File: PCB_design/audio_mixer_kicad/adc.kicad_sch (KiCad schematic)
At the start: 10 parts, among them U10 TLV320ADC3140IRTWR

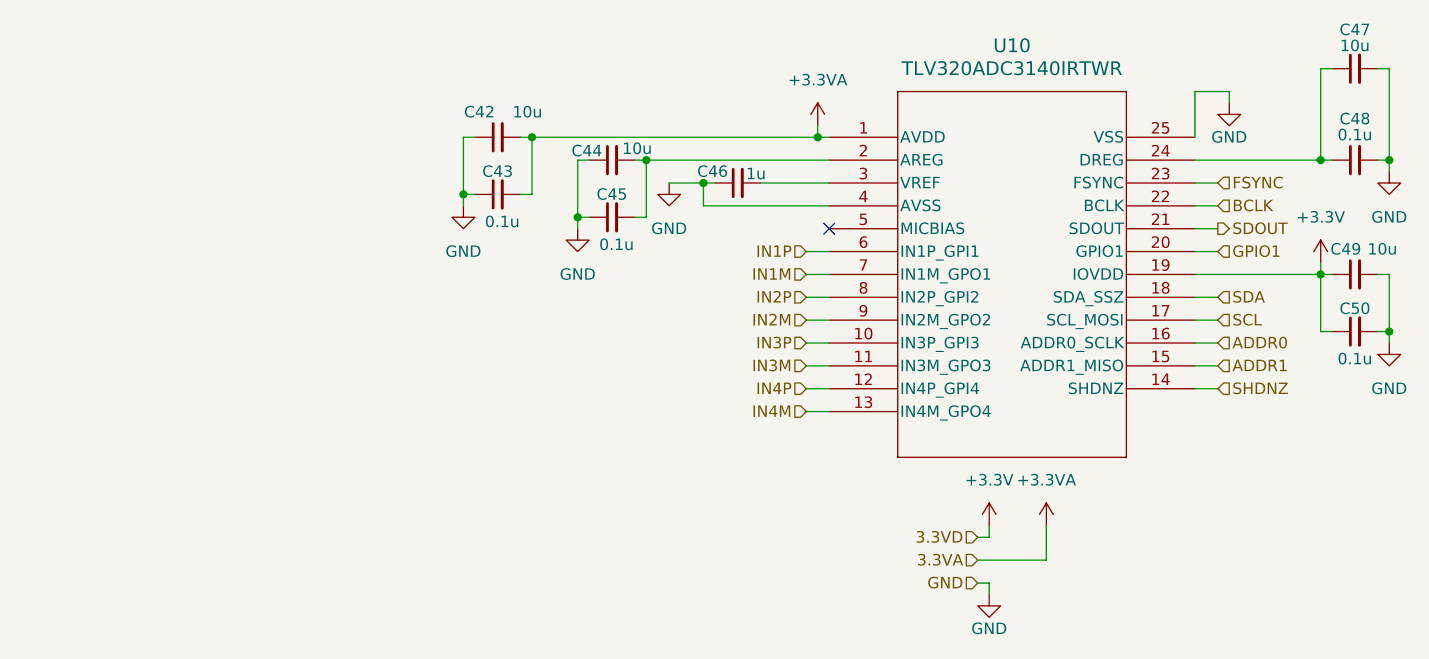
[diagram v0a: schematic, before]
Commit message: Add oscillator and adc input caps
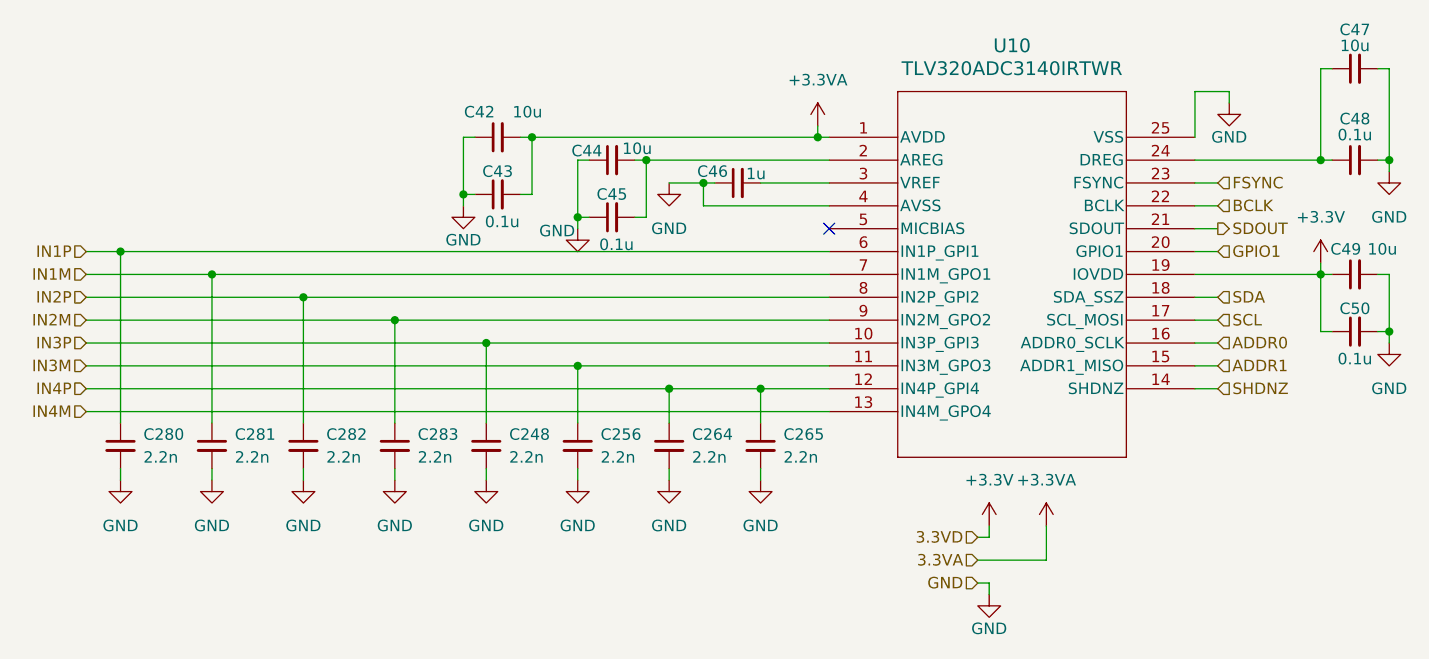
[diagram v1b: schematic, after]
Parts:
- added C248, C256, C264, C265, C280, C281, C282, C283: 2.2n, symbol Device:C_Small
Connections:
- net GND: now also C248.2, C256.2, C264.2, C265.2, C280.2, C281.2, C282.2, C283.2
- net IN1M: now also C281.1
- net IN1P: now also C280.1
- net IN2M: now also C283.1
- net IN2P: now also C282.1
- net IN3M: now also C256.1
- net IN3P: now also C248.1
- net IN4P: now also C264.1, C265.1

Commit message: Reannotate and add passives for Y1
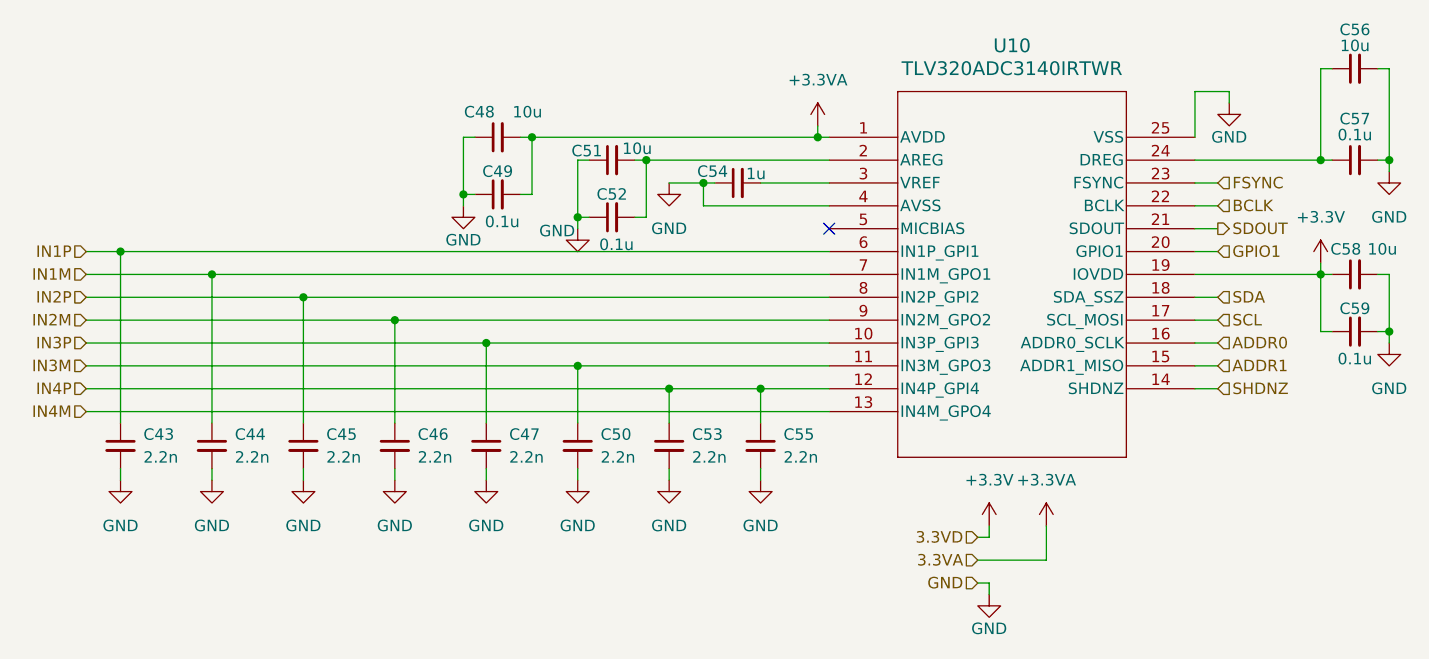
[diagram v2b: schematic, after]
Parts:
- renumbered C280 to C43, C281 to C44, C282 to C45, C283 to C46, C248 to C47, C42 to C48, C43 to C49, C256 to C50, C44 to C51, C45 to C52, C264 to C53, C46 to C54, C265 to C55, C47 to C56, C48 to C57, C49 to C58, C50 to C59
